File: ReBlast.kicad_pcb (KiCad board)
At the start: 2 copper layers, 50.7 x 64.9 mm, 23 parts, among them J1 MOS_8580_Socket, U1 74HC20, U2 74HC139, U3 ZN428E-8, U4 TLC272, U5 MOS_8580, U6 ADC0804

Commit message: Fix DRC
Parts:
- moved C7 0.25 mm to (150.7, 80.5)
- moved R2 0.17 mm to (164.7, 80.5)
- moved C2 0.17 mm to (169.8, 80.5)
- moved D1 0.17 mm to (172.3, 84.3)

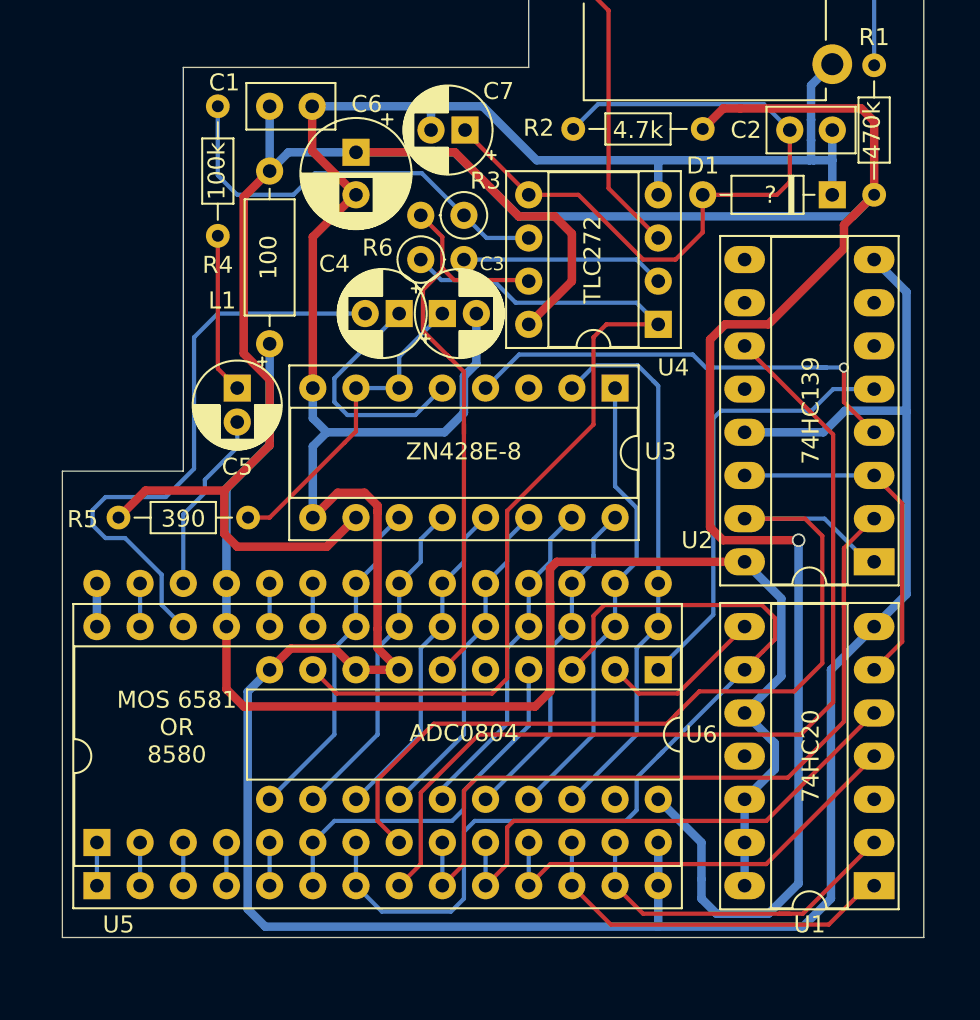
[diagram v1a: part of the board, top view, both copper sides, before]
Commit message: Add some notes, fix ERC, adjust some tracks
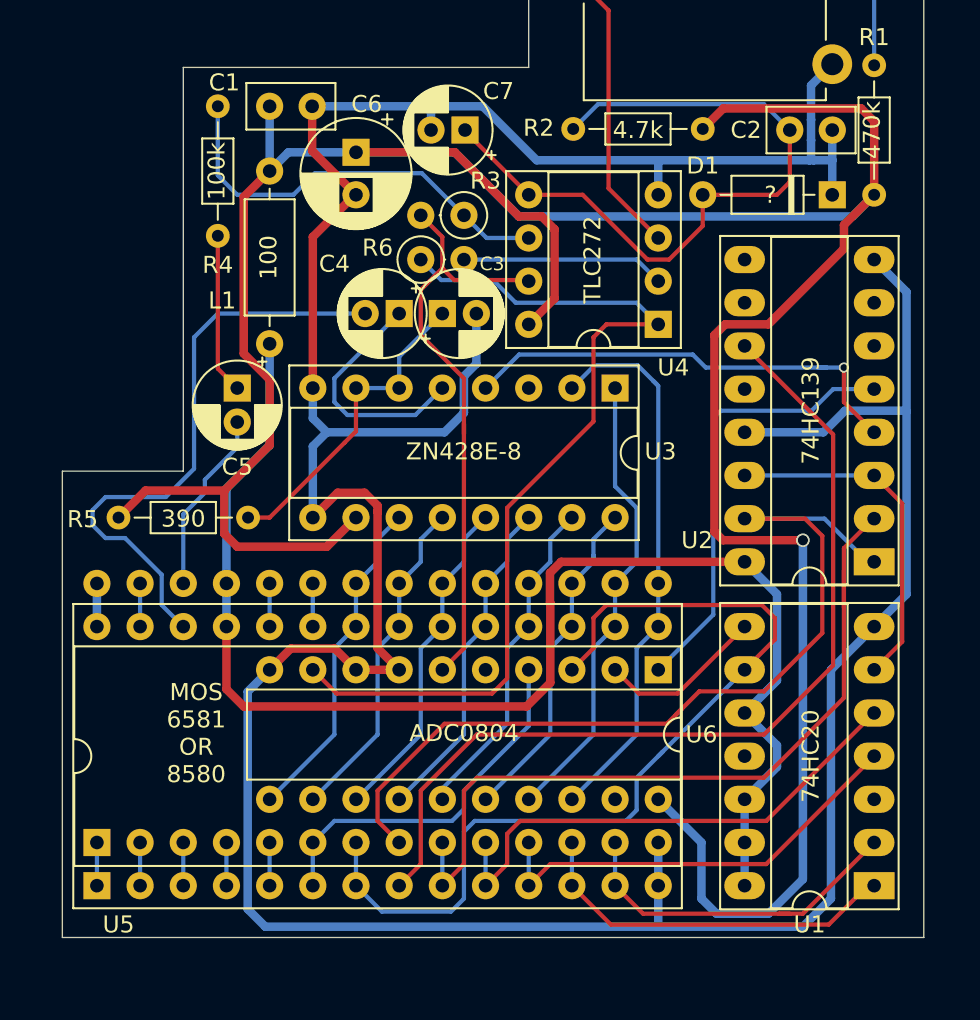
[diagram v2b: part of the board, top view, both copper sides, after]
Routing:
- net /~cs_in: track 54.9 -> 53.5 mm
- net /~cs_sid: track 55.6 -> 54.4 mm
- net +5V: track 182.0 -> 180.9 mm
- net /a0: track 47.5 -> 46.7 mm
- net VCC: track 82.4 -> 81.8 mm

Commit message: AT LAAAAAAAAAST! Though I must admit that R6 is really misleading...
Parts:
- C5: value CP1 -> 1u
- D1: value 2.5V ZENER -> 1n4148
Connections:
- C2 pad 1: Net-(C2-Pad1) -> /adc_vref_half
- C7 pad 1: Net-(C2-Pad1) -> /opamp_bias
- D1 pad 2: Net-(C2-Pad1) -> /adc_vref_half
- R2 pad 2: Net-(C2-Pad1) -> /adc_vref_half
- R6 pad 1: /adc_vref_half -> Net-(R6-Pad1)
- RV1 pad 2: Net-(RV1-Pad2) -> /opamp_bias
- U4 pad 1: /adc_vref_half -> Net-(R6-Pad1)
- U4 pad 3: Net-(RV1-Pad2) -> /opamp_bias
- U4 pad 5: Net-(C2-Pad1) -> /opamp_bias
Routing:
- net Net-(C2-Pad1): track 42.1 -> 0.00 mm
- net /opamp_bias: track 0.00 -> 27.4 mm
- net Net-(RV1-Pad2): track 17.2 -> 0.00 mm
- net Net-(R6-Pad1): track 0.00 -> 15.5 mm
- net /adc_vref_half: track 54.2 -> 69.4 mm
- net GNDA: track 215.7 -> 215.1 mm
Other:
- board text removed: "?"

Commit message: Almost there...
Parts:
- removed R6: 330k, Resistor_THT:R_Axial_DIN0207_L6.3mm_D2.5mm_P2.54mm_Vertical
- added C10: 100n, Capacitor_THT:C_Disc_D7.0mm_W2.5mm_P5.00mm, F.Cu at (165.2, 108.8)
- added C8: 100n, Capacitor_THT:C_Disc_D7.0mm_W2.5mm_P5.00mm, F.Cu at (165.2, 116.4)
- added C9: 100n, Capacitor_THT:C_Disc_D7.0mm_W2.5mm_P5.00mm, F.Cu at (165.2, 97.3)
- C1, C2: footprint Capacitor_THT:C_Disc_D5.0mm_W2.5mm_P2.50mm -> Capacitor_THT:C_Disc_D7.0mm_W2.5mm_P5.00mm
- D1: footprint Diode_THT:D_DO-35_SOD27_P7.62mm_Horizontal -> Diode_THT:D_DO-35_SOD27_P2.54mm_Vertical_KathodeUp
- L1: footprint Inductor_THT:L_Axial_L6.6mm_D2.7mm_P10.16mm_Horizontal_Vishay_IM-2 -> Inductor_THT:L_Radial_D6.0mm_P4.00mm
- R1, R2, R4, R5: footprint Resistor_THT:R_Axial_DIN0204_L3.6mm_D1.6mm_P7.62mm_Horizontal -> Resistor_THT:R_Axial_DIN0207_L6.3mm_D2.5mm_P2.54mm_Vertical
- RV1: footprint Potentiometer_THT:Potentiometer_ACP_CA14V-15_Vertical -> ReBlast:Pot_Bourns_3306P
- moved D1 37.8 mm to (137.3, 70.1), turned to 270 degrees
- moved C2 29.2 mm to (141.1, 75.1), turned to 90 degrees
- moved R2 27.5 mm to (137.3, 77.7), turned to 90 degrees
- moved C1 19.8 mm to (157.7, 71.9)
- moved R4 18.0 mm to (153.8, 75.8), turned to 180 degrees
- moved R5 12.3 mm to (139.2, 94.7), turned to 90 degrees
- moved R1 11.1 mm to (167.8, 75.8)
- moved C4 10.5 mm to (146.2, 80.8), turned to 0 degrees
- moved L1 10.4 mm to (141.1, 82.8)
- moved C7 8.95 mm to (153.3, 71.9)
- moved C3 8.78 mm to (151.3, 82.7)
- moved C5 8.78 mm to (139.2, 87.1)
- moved C6 8.78 mm to (146.2, 73.3)
- moved U1 8.78 mm to (176.7, 116.4)
- moved U2 8.78 mm to (176.7, 97.3)
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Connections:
- R3 pad 1: Net-(R3-Pad1) -> /adc_in
- R3 pad 2: /adc_in -> Net-(R3-Pad2)
- R4 pad 1: Net-(R3-Pad1) -> Net-(R3-Pad2)
- U4 pad 1: Net-(R6-Pad1) -> Net-(U4-Pad1)
- U4 pad 2: Net-(R6-Pad2) -> Net-(U4-Pad1)
- U4 pad 6: Net-(R3-Pad1) -> Net-(R3-Pad2)
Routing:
- net GNDA: track 215.1 -> 0.00 mm, vias 0 -> 1
- net +5V: track 180.9 -> 139.3 mm
- net /adc_vref_half: track 69.4 -> 37.3 mm
- net Net-(R3-Pad1): track 24.9 -> 0.00 mm
- net /adc_in: track 35.4 -> 54.1 mm
- net /r_~w: track 54.4 -> 38.5 mm, vias 0 -> 1
- net Net-(R6-Pad1): track 15.5 -> 0.00 mm
- net Net-(R6-Pad2): track 12.0 -> 0.00 mm
- net /~cs_in: track 53.5 -> 64.3 mm, vias 0 -> 1
- net Net-(C5-Pad1): track 9.43 -> 19.6 mm
- net VCC: track 81.8 -> 89.7 mm
- net Net-(R3-Pad2): track 0.00 -> 5.08 mm
- net /audio_in: track 35.1 -> 31.1 mm
- net Net-(R1-Pad2): track 11.0 -> 7.17 mm
- net /~cs_sid: track 54.4 -> 57.8 mm
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- added copper zone on B.Cu, net GNDA
- added copper zone on F.Cu, net GNDA
- removed copper zone on B.Cu, net GNDD
- removed copper zone on F.Cu, net GNDD
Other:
- board size 50.7 x 64.9 mm -> 52.3 x 51.8 mm
- board text added: "V1"

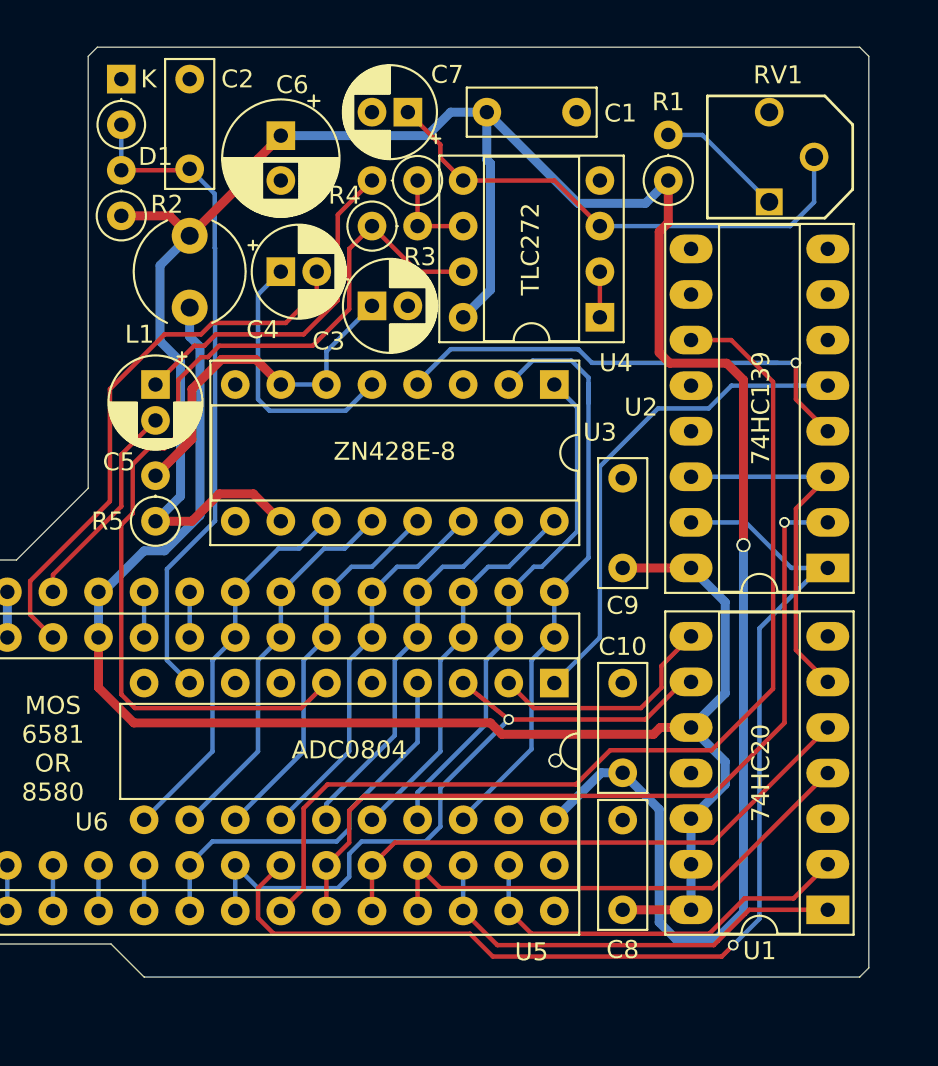
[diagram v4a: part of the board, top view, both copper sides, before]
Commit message: Better ground plane
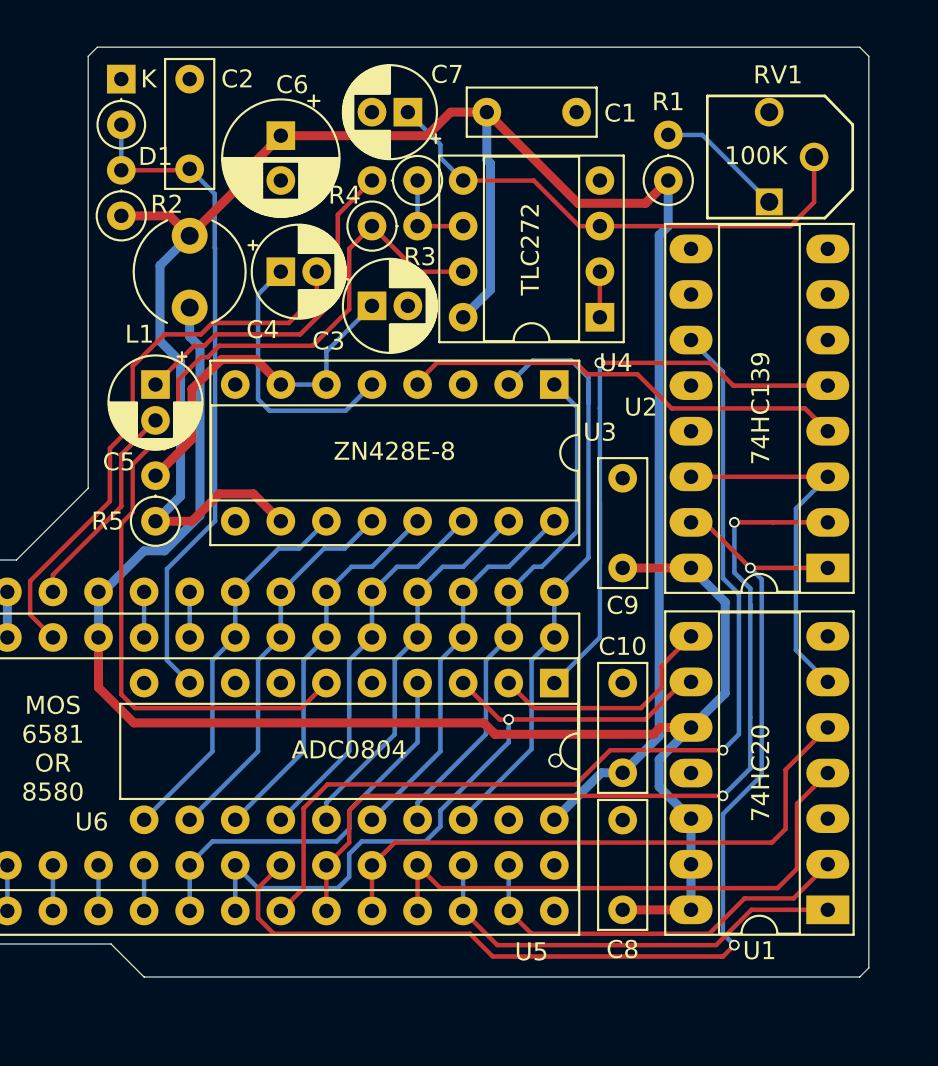
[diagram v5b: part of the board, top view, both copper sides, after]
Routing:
- net +5V: track 139.3 -> 113.7 mm, vias 1 -> 0
- net /~cs_adc: track 27.7 -> 35.5 mm, vias 0 -> 1
- net /a0: track 46.0 -> 49.2 mm, vias 1 -> 2
- net /~cs_sid: track 57.8 -> 55.3 mm, vias 0 -> 1
- net /~cs_dac: track 27.3 -> 25.0 mm, vias 1 -> 0
- net /a2: track 28.6 -> 30.7 mm
- net /a1: track 31.1 -> 33.1 mm
- net /~cs_in: track 64.3 -> 63.3 mm, vias 1 -> 2

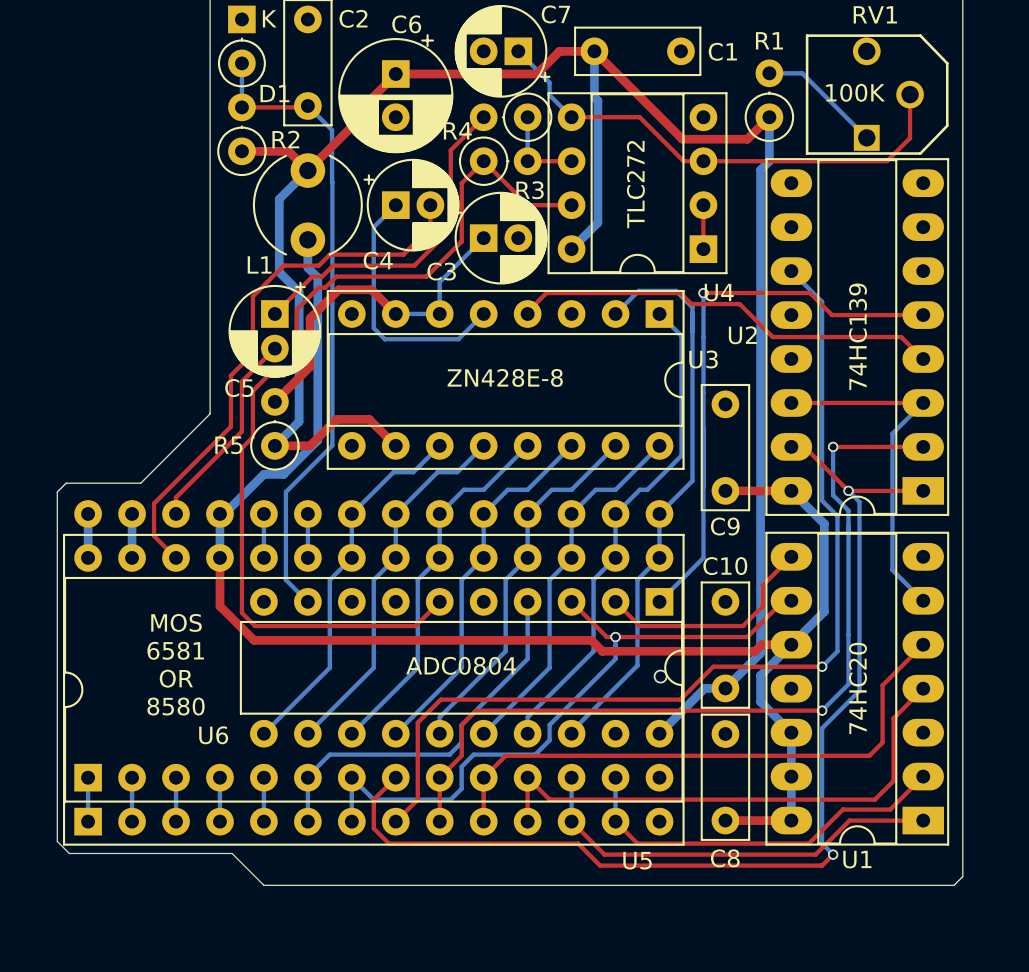
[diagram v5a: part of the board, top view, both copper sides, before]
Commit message: Center U6 within U5
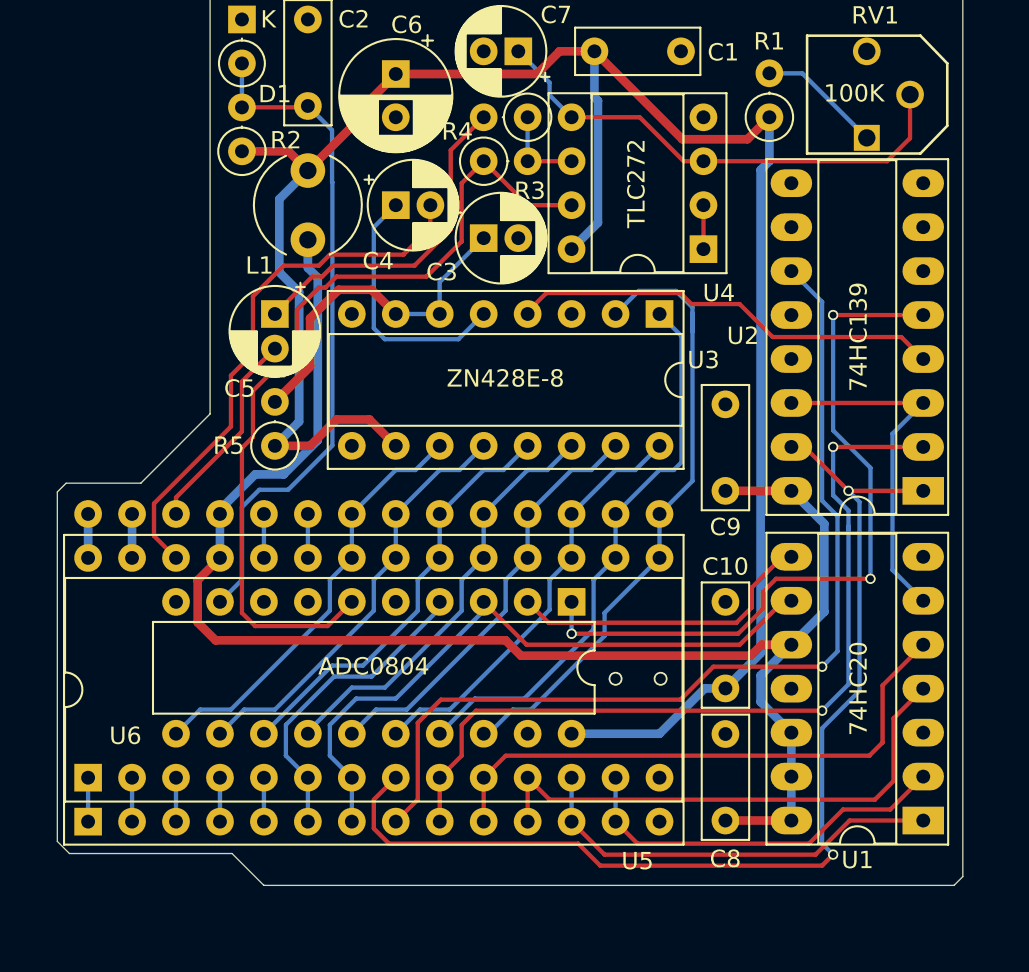
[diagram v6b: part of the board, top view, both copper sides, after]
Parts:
- moved U6 5.08 mm to (156.3, 103.8)
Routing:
- net /~cs_adc: track 35.5 -> 42.3 mm, vias 1 -> 3
- net +5V: track 113.7 -> 118.8 mm
- net /adc_in: track 54.1 -> 49.1 mm
- net /~read: track 13.1 -> 18.0 mm
- net /d1: track 28.7 -> 32.7 mm
- net /phi2: track 22.0 -> 18.2 mm
- net /d4: track 21.5 -> 24.7 mm
- net /d5: track 21.5 -> 24.7 mm
- net /d6: track 21.5 -> 24.7 mm
- net /d3: track 21.5 -> 24.7 mm
- net /d7: track 21.5 -> 24.7 mm
- net /d2: track 21.5 -> 24.6 mm
- net /d0: track 34.0 -> 36.9 mm
- net VCC: track 89.6 -> 92.4 mm
- net /adc_vref_half: track 37.3 -> 39.3 mm
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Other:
- board text removed: "MOS 6581 OR 8580"

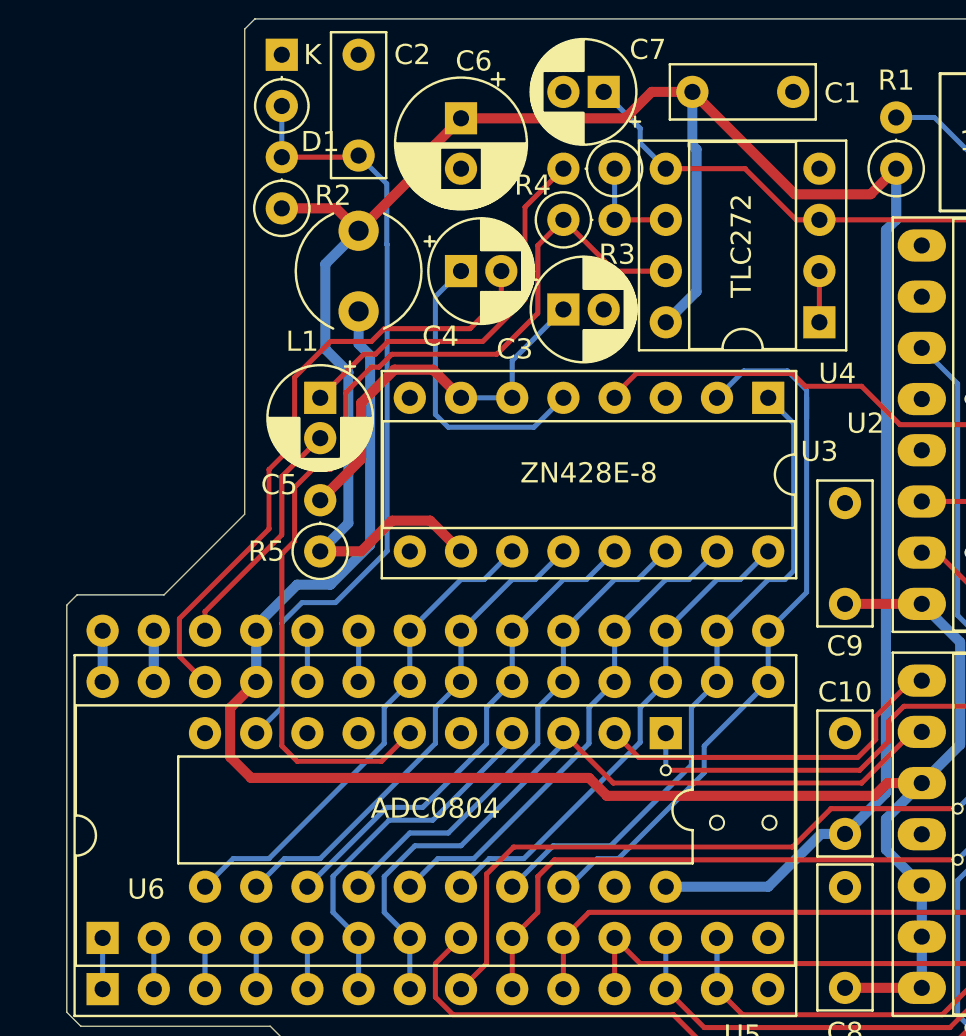
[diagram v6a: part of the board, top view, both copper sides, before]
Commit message: Add logo, etc.
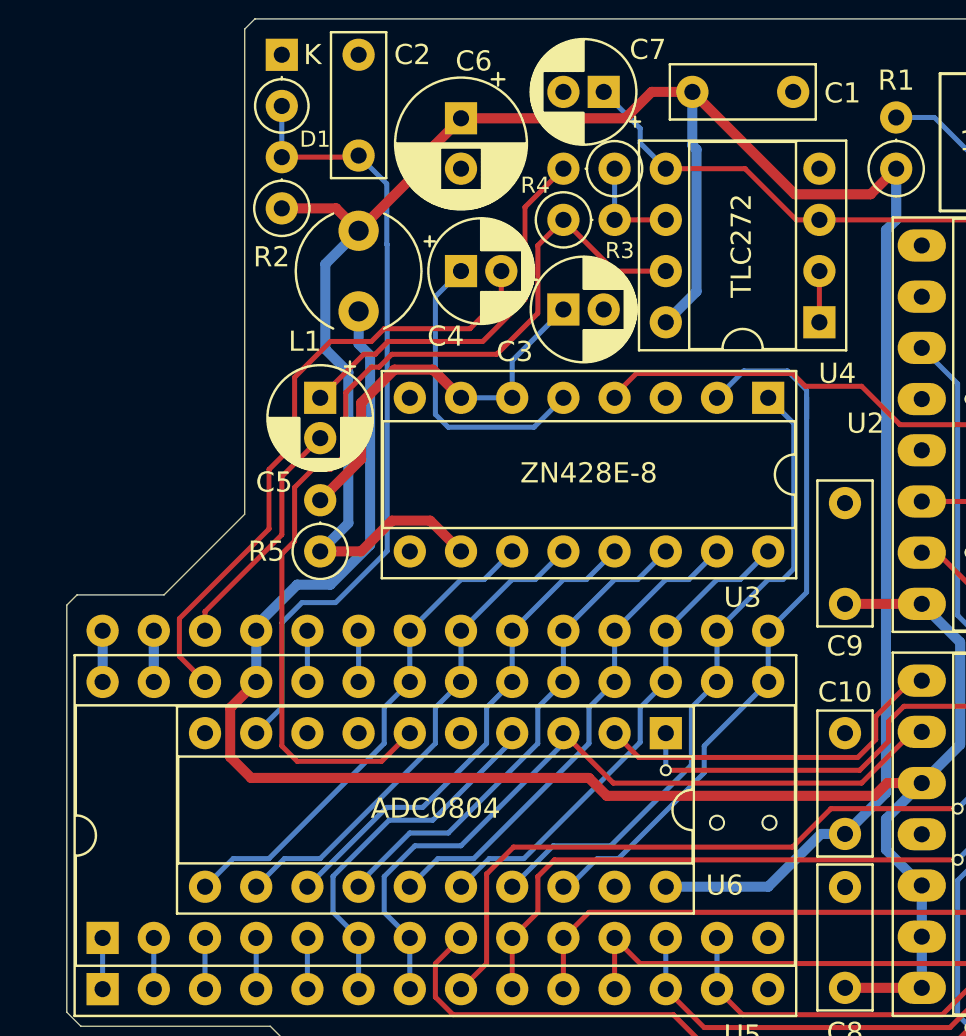
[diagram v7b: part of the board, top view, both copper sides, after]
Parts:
- added V0: LOGO, ReBlast:logo, B.Cu at (152.5, 90.9)
- added V1: LICENSE, ReBlast:cc_by_nc_sa_small, B.Cu at (160.1, 78.5)
- U6: footprint Package_DIP:DIP-20_W7.62mm -> Package_DIP:DIP-20_W7.62mm_Socket
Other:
- board text added: "Based on work by Solder/Synergy github.com/SukkoPera/ReBlast"
- board text added: "CC-BY-NC-SA ©SukkoPera 2024"
